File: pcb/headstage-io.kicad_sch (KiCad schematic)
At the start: 2 parts, among them J1 BSE-040-01-X-D-A

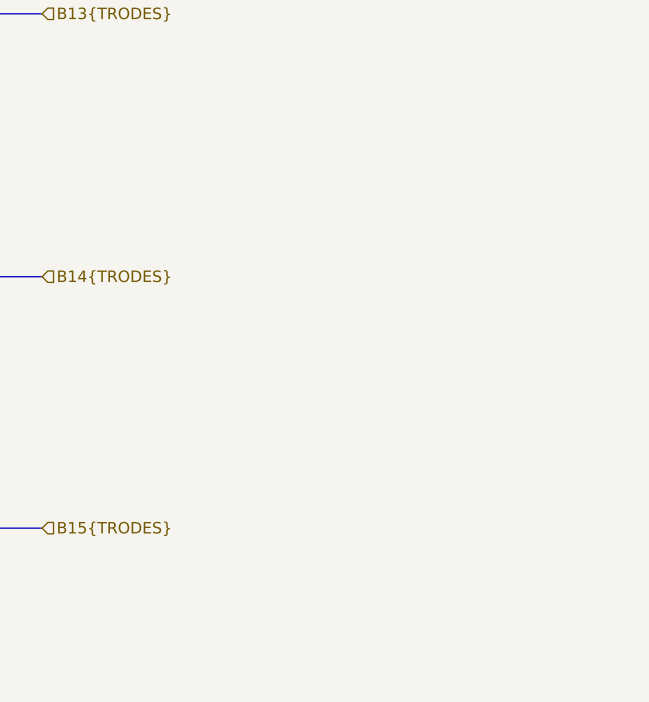
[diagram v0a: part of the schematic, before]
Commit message: Remove battery power option
- This device needs user IO
- Battery power means there would need to be a touch screen or wireless
  connection. Too complex.
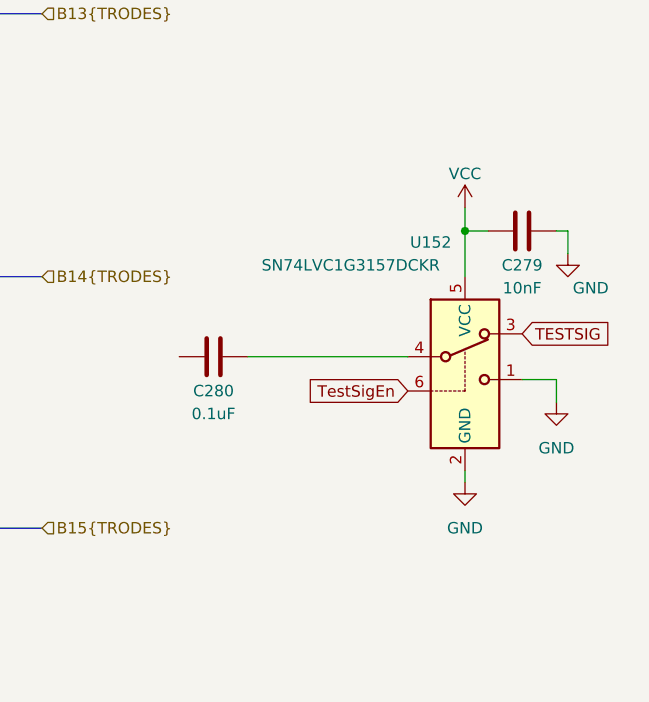
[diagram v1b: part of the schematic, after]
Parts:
- added C279: 10nF, Capacitor_SMD:C_0402_1005Metric, symbol Device:C
- added C280: 0.1uF, Capacitor_SMD:C_0402_1005Metric, symbol Device:C
- added U152: SN74LVC1G3157DCKR, Package_TO_SOT_SMD:SOT-363_SC-70-6, symbol open-ephys:SN74LVC1G3157DCKR
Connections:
- net GND: now also C279.2, U152.1, U152.2 (GND)
- new net: C280.2, U152.4
- new net TESTSIG: U152.3
- new net TestSigEn: U152.6
- new net VCC: C279.1, U152.5 (VCC)

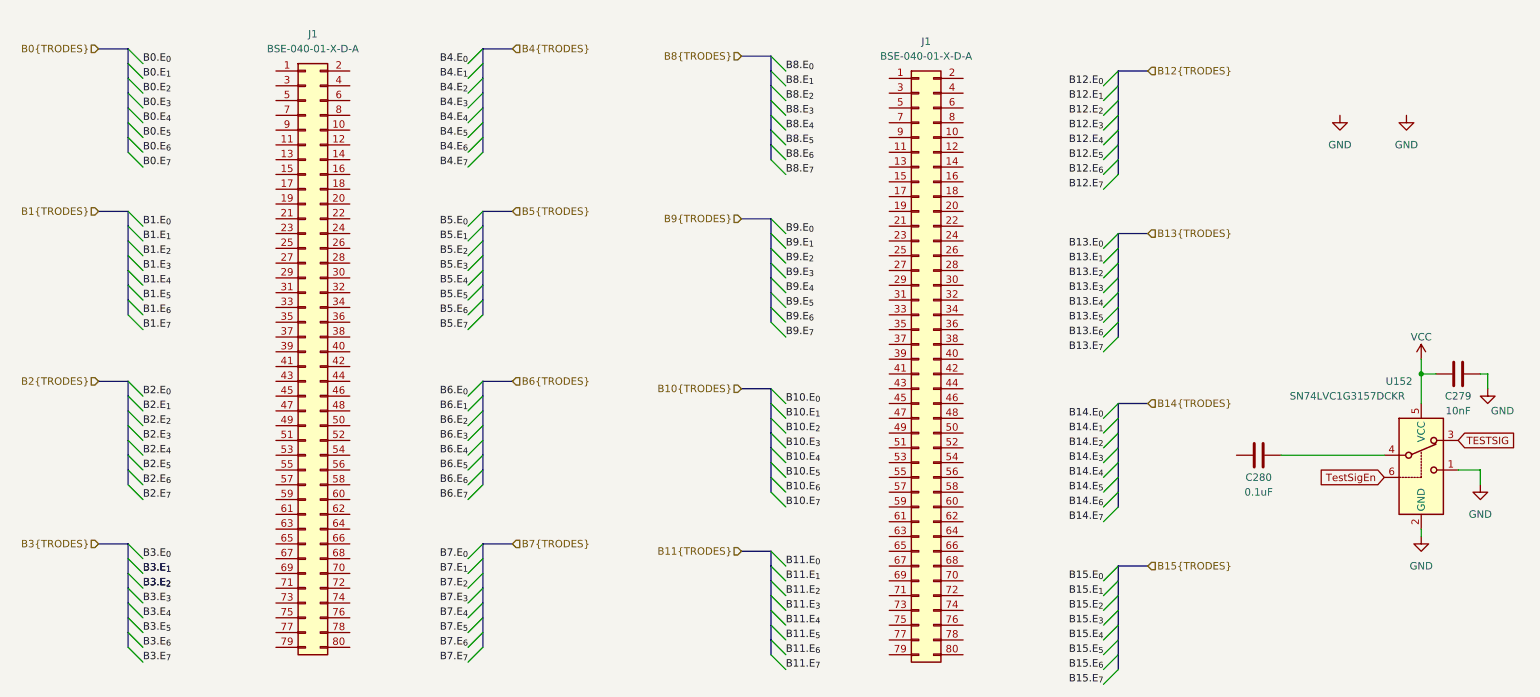
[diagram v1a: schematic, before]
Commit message: Finished schematic, started routing
- There is a 8-channel motif that will need to be copied 16x on the
  board. I'm not sure the most efficient way to do this.
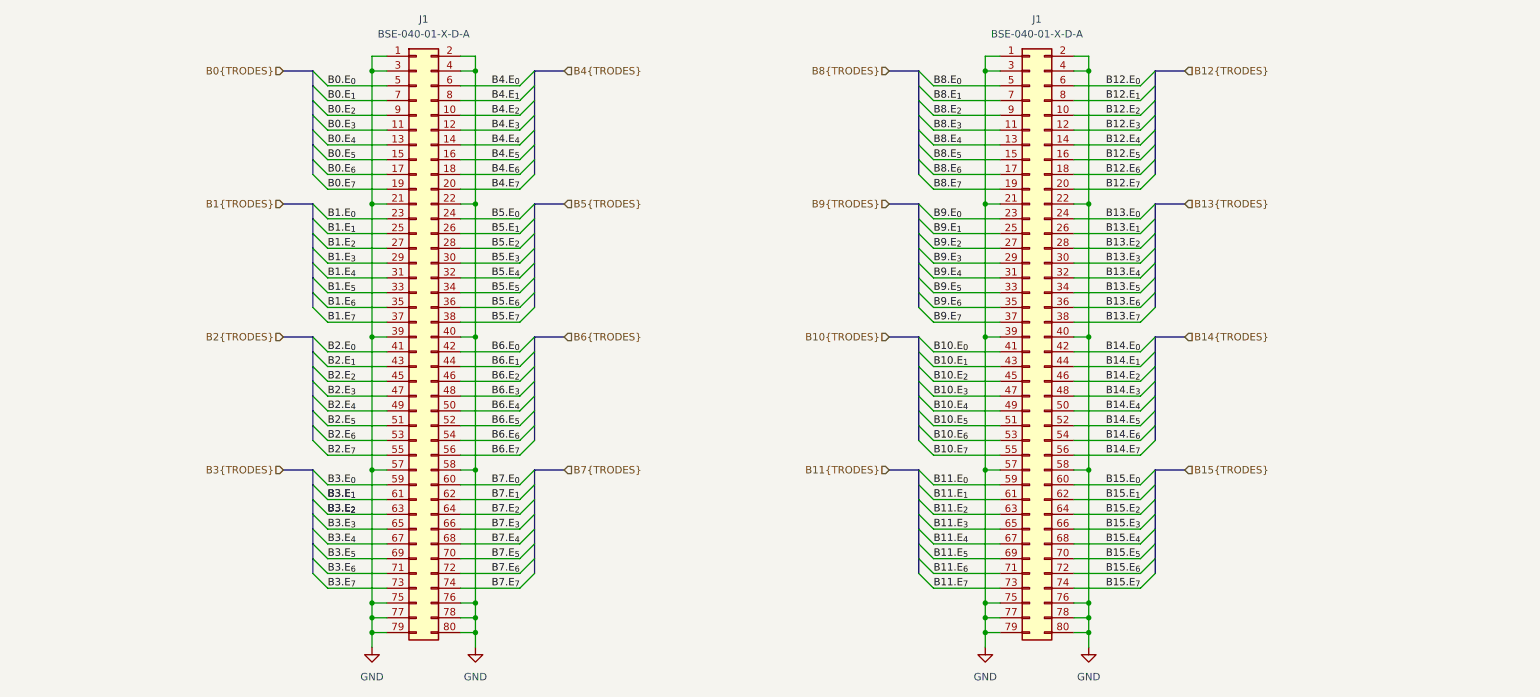
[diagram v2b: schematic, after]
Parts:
- removed C279: 10nF, Capacitor_SMD:C_0402_1005Metric, symbol Device:C
- removed C280: 0.1uF, Capacitor_SMD:C_0402_1005Metric, symbol Device:C
- removed U152: SN74LVC1G3157DCKR, Package_TO_SOT_SMD:SOT-363_SC-70-6, symbol open-ephys:SN74LVC1G3157DCKR
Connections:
- net B0.E_{0}: now also J1.5 (Pin_5)
- net B0.E_{1}: now also J1.7 (Pin_7)
- net B0.E_{2}: now also J1.9 (Pin_9)
- net B0.E_{3}: now also J1.11 (Pin_11)
- net B0.E_{4}: now also J1.13 (Pin_13)
- net B0.E_{5}: now also J1.15 (Pin_15)
- net B0.E_{6}: now also J1.17 (Pin_17)
- net B0.E_{7}: now also J1.19 (Pin_19)
- net B1.E_{0}: now also J1.23 (Pin_23)
- net B1.E_{1}: now also J1.25 (Pin_25)
- net B1.E_{2}: now also J1.27 (Pin_27)
- net B1.E_{3}: now also J1.29 (Pin_29)
- net B1.E_{4}: now also J1.31 (Pin_31)
- net B1.E_{5}: now also J1.33 (Pin_33)
- net B1.E_{6}: now also J1.35 (Pin_35)
- net B1.E_{7}: now also J1.37 (Pin_37)
- net B10.E_{0}: now also J1.41 (Pin_41)
- net B10.E_{1}: now also J1.43 (Pin_43)
- net B10.E_{2}: now also J1.45 (Pin_45)
- net B10.E_{3}: now also J1.47 (Pin_47)
- net B10.E_{4}: now also J1.49 (Pin_49)
- net B10.E_{5}: now also J1.51 (Pin_51)
- net B10.E_{6}: now also J1.53 (Pin_53)
- net B10.E_{7}: now also J1.55 (Pin_55)
- net B11.E_{0}: now also J1.59 (Pin_59)
- net B11.E_{1}: now also J1.61 (Pin_61)
- net B11.E_{2}: now also J1.63 (Pin_63)
- net B11.E_{3}: now also J1.65 (Pin_65)
- net B11.E_{4}: now also J1.67 (Pin_67)
- net B11.E_{5}: now also J1.69 (Pin_69)
- net B11.E_{6}: now also J1.71 (Pin_71)
- net B11.E_{7}: now also J1.73 (Pin_73)
- net B12.E_{0}: now also J1.6 (Pin_6)
- net B12.E_{1}: now also J1.8 (Pin_8)
- net B12.E_{2}: now also J1.10 (Pin_10)
- net B12.E_{3}: now also J1.12 (Pin_12)
- net B12.E_{4}: now also J1.14 (Pin_14)
- net B12.E_{5}: now also J1.16 (Pin_16)
- net B12.E_{6}: now also J1.18 (Pin_18)
- net B12.E_{7}: now also J1.20 (Pin_20)
- net B13.E_{0}: now also J1.24 (Pin_24)
- net B13.E_{1}: now also J1.26 (Pin_26)
- net B13.E_{2}: now also J1.28 (Pin_28)
- net B13.E_{3}: now also J1.30 (Pin_30)
- net B13.E_{4}: now also J1.32 (Pin_32)
- net B13.E_{5}: now also J1.34 (Pin_34)
- net B13.E_{6}: now also J1.36 (Pin_36)
- net B13.E_{7}: now also J1.38 (Pin_38)
- net B14.E_{0}: now also J1.42 (Pin_42)
- net B14.E_{1}: now also J1.44 (Pin_44)
- net B14.E_{2}: now also J1.46 (Pin_46)
- net B14.E_{3}: now also J1.48 (Pin_48)
- net B14.E_{4}: now also J1.50 (Pin_50)
- net B14.E_{5}: now also J1.52 (Pin_52)
- net B14.E_{6}: now also J1.54 (Pin_54)
- net B14.E_{7}: now also J1.56 (Pin_56)
- net B15.E_{0}: now also J1.60 (Pin_60)
- net B15.E_{1}: now also J1.62 (Pin_62)
- net B15.E_{2}: now also J1.64 (Pin_64)
- net B15.E_{3}: now also J1.66 (Pin_66)
- net B15.E_{4}: now also J1.68 (Pin_68)
- net B15.E_{5}: now also J1.70 (Pin_70)
- net B15.E_{6}: now also J1.72 (Pin_72)
- net B15.E_{7}: now also J1.74 (Pin_74)
- net B2.E_{0}: now also J1.41 (Pin_41)
- net B2.E_{1}: now also J1.43 (Pin_43)
- net B2.E_{2}: now also J1.45 (Pin_45)
- net B2.E_{3}: now also J1.47 (Pin_47)
- net B2.E_{4}: now also J1.49 (Pin_49)
- net B2.E_{5}: now also J1.51 (Pin_51)
- net B2.E_{6}: now also J1.53 (Pin_53)
- net B2.E_{7}: now also J1.55 (Pin_55)
- net B3.E_{0}: now also J1.59 (Pin_59)
- net B3.E_{1}: now also J1.61 (Pin_61)
- net B3.E_{2}: now also J1.63 (Pin_63)
- net B3.E_{3}: now also J1.65 (Pin_65)
- net B3.E_{4}: now also J1.67 (Pin_67)
- net B3.E_{5}: now also J1.69 (Pin_69)
- net B3.E_{6}: now also J1.71 (Pin_71)
- net B3.E_{7}: now also J1.73 (Pin_73)
- net B4.E_{0}: now also J1.6 (Pin_6)
- net B4.E_{1}: now also J1.8 (Pin_8)
- net B4.E_{2}: now also J1.10 (Pin_10)
- net B4.E_{3}: now also J1.12 (Pin_12)
- net B4.E_{4}: now also J1.14 (Pin_14)
- net B4.E_{5}: now also J1.16 (Pin_16)
- net B4.E_{6}: now also J1.18 (Pin_18)
- net B4.E_{7}: now also J1.20 (Pin_20)
- net B5.E_{0}: now also J1.24 (Pin_24)
- net B5.E_{1}: now also J1.26 (Pin_26)
- net B5.E_{2}: now also J1.28 (Pin_28)
- net B5.E_{3}: now also J1.30 (Pin_30)
- net B5.E_{4}: now also J1.32 (Pin_32)
- net B5.E_{5}: now also J1.34 (Pin_34)
- net B5.E_{6}: now also J1.36 (Pin_36)
- net B5.E_{7}: now also J1.38 (Pin_38)
- net B6.E_{0}: now also J1.42 (Pin_42)
- net B6.E_{1}: now also J1.44 (Pin_44)
- net B6.E_{2}: now also J1.46 (Pin_46)
- net B6.E_{3}: now also J1.48 (Pin_48)
- net B6.E_{4}: now also J1.50 (Pin_50)
- net B6.E_{5}: now also J1.52 (Pin_52)
- net B6.E_{6}: now also J1.54 (Pin_54)
- net B6.E_{7}: now also J1.56 (Pin_56)
- net B7.E_{0}: now also J1.60 (Pin_60)
- net B7.E_{1}: now also J1.62 (Pin_62)
- net B7.E_{2}: now also J1.64 (Pin_64)
- net B7.E_{3}: now also J1.66 (Pin_66)
- net B7.E_{4}: now also J1.68 (Pin_68)
- net B7.E_{5}: now also J1.70 (Pin_70)
- net B7.E_{6}: now also J1.72 (Pin_72)
- net B7.E_{7}: now also J1.74 (Pin_74)
- net B8.E_{0}: now also J1.5 (Pin_5)
- net B8.E_{1}: now also J1.7 (Pin_7)
- net B8.E_{2}: now also J1.9 (Pin_9)
- net B8.E_{3}: now also J1.11 (Pin_11)
- net B8.E_{4}: now also J1.13 (Pin_13)
- net B8.E_{5}: now also J1.15 (Pin_15)
- net B8.E_{6}: now also J1.17 (Pin_17)
- net B8.E_{7}: now also J1.19 (Pin_19)
- net B9.E_{0}: now also J1.23 (Pin_23)
- net B9.E_{1}: now also J1.25 (Pin_25)
- net B9.E_{2}: now also J1.27 (Pin_27)
- net B9.E_{3}: now also J1.29 (Pin_29)
- net B9.E_{4}: now also J1.31 (Pin_31)
- net B9.E_{5}: now also J1.33 (Pin_33)
- net B9.E_{6}: now also J1.35 (Pin_35)
- net B9.E_{7}: now also J1.37 (Pin_37)
- net GND: now also J1.1 (Pin_1), J1.1 (Pin_1), J1.2 (Pin_2), J1.2 (Pin_2), J1.21 (Pin_21), J1.21 (Pin_21), J1.22 (Pin_22), J1.22 (Pin_22), J1.3 (Pin_3), J1.3 (Pin_3), J1.39 (Pin_39), J1.39 (Pin_39), J1.4 (Pin_4), J1.4 (Pin_4), J1.40 (Pin_40), J1.40 (Pin_40), J1.57 (Pin_57), J1.57 (Pin_57), J1.58 (Pin_58), J1.58 (Pin_58), J1.75 (Pin_75), J1.75 (Pin_75), J1.76 (Pin_76), J1.76 (Pin_76), J1.77 (Pin_77), J1.77 (Pin_77), J1.78 (Pin_78), J1.78 (Pin_78), J1.79 (Pin_79), J1.79 (Pin_79), J1.80 (Pin_80), J1.80 (Pin_80)
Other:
- moved on the sheet: J1

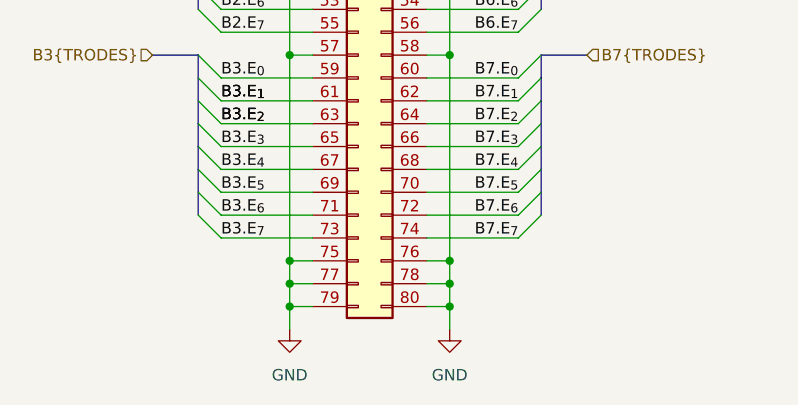
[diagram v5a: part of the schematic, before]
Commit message: Add EEPROM support to headstage interface
- I2C + Power
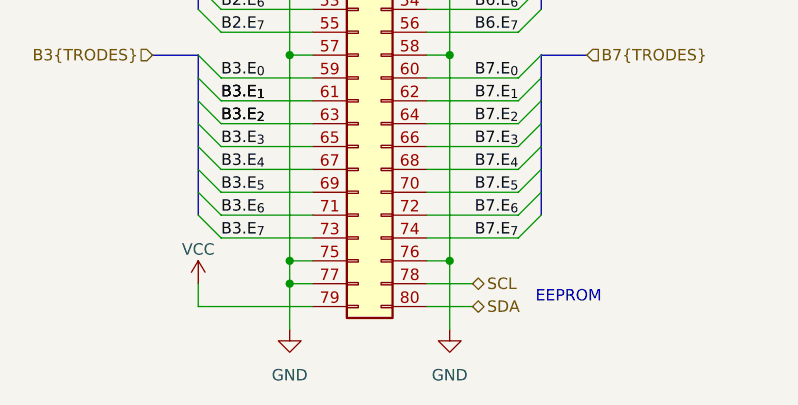
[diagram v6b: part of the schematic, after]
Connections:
- net GND: no longer J1.78 (Pin_78), J1.79 (Pin_79), J1.80 (Pin_80)
- new net SCL: J1.78 (Pin_78)
- new net SDA: J1.80 (Pin_80)
- new net VCC: J1.79 (Pin_79)
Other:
- note added: "EEPROM"
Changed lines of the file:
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@@
 	)
 	(junction
-		(at 96.52 140.97)
-		(diameter 0)
-		(color 0 0 0 0)
-	)
-	(junction
 		(at 201.93 92.71)
 		(diameter 0)
@@
 	)
 	(junction
-		(at 201.93 69.85)
+		(at 78.74 140.97)
 		(diameter 0)
 		(color 0 0 0 0)
 	)
 	(junction
-		(at 78.74 143.51)
+		(at 201.93 69.85)
 		(diameter 0)
 		(color 0 0 0 0)
@@
 		(color 0 0 0 0)
 	)
-	(junction
-		(at 96.52 143.51)
-		(diameter 0)
-		(color 0 0 0 0)
-	)
-	(junction
-		(at 78.74 140.97)
-		(diameter 0)
-		(color 0 0 0 0)
-	)
 	(bus_entry
 		(at 68.58 100.33)
@@
 	(wire
 		(pts
-			(xy 78.74 138.43) (xy 78.74 140.97)
+			(xy 68.58 143.51) (xy 68.58 140.97)
 		)
 		(stroke
@@
 	(wire
 		(pts
+			(xy 93.98 140.97) (xy 99.06 140.97)
+		)
+		(stroke
+			(width 0)
+			(type default)
+		)
+	)
+	(wire
+		(pts
 			(xy 199.39 62.23) (xy 210.82 62.23)
 		)
@@
 	(wire
 		(pts
-			(xy 78.74 143.51) (xy 78.74 146.05)
+			(xy 78.74 138.43) (xy 78.74 140.97)
 		)
 		(stroke
@@
 	(wire
 		(pts
+			(xy 78.74 140.97) (xy 78.74 146.05)
+		)
+		(stroke
+			(width 0)
+			(type default)
+		)
+	)
+	(wire
+		(pts
 			(xy 71.12 130.81) (xy 81.28 130.81)
 		)
@@
 	(wire
 		(pts
+			(xy 93.98 143.51) (xy 99.06 143.51)
+		)
+		(stroke
+			(width 0)
+			(type default)
+		)
+	)
+	(wire
+		(pts
 			(xy 96.52 115.57) (xy 96.52 138.43)
 		)
@@
 	(wire
 		(pts
-			(xy 96.52 140.97) (xy 96.52 143.51)
+			(xy 96.52 138.43) (xy 96.52 146.05)
 		)
 		(stroke
@@
 		)
 	)
-	(wire
-		(pts
-			(xy 78.74 140.97) (xy 78.74 143.51)
-		)
-		(stroke
-			(width 0)
-			(type default)
-		)
-	)
 	(bus
 		(pts
@@
 	(wire
 		(pts
-			(xy 93.98 143.51) (xy 96.52 143.51)
-		)
-		(stroke
-			(width 0)
-			(type default)
-		)
-	)
-	(wire
-		(pts
 			(xy 199.39 120.65) (xy 210.82 120.65)
 		)
@@
 		)
 	)
-	(wire
-		(pts
-			(xy 78.74 143.51) (xy 81.28 143.51)
-		)
-		(stroke
-			(width 0)
-			(type default)
-		)
-	)
 	(bus
 		(pts
@@
 		)
 	)
-	(wire
-		(pts
-			(xy 78.74 140.97) (xy 81.28 140.97)
-		)
-		(stroke
-			(width 0)
-			(type default)
-		)
-	)
 	(bus
 		(pts
@@
 	(wire
 		(pts
-			(xy 93.98 140.97) (xy 96.52 140.97)
-		)
-		(stroke
-			(width 0)
-			(type default)
-		)
-	)
-	(wire
-		(pts
 			(xy 71.12 118.11) (xy 81.28 118.11)
 		)
@@
 	(wire
 		(pts
+			(xy 78.74 140.97) (xy 81.28 140.97)
+		)
+		(stroke
+			(width 0)
+			(type default)
+		)
+	)
+	(wire
+		(pts
 			(xy 199.39 125.73) (xy 210.82 125.73)
 		)
@@
 	(wire
 		(pts
+			(xy 81.28 143.51) (xy 68.58 143.51)
+		)
+		(stroke
+			(width 0)
+			(type default)
+		)
+	)
+	(wire
+		(pts
 			(xy 175.26 57.15) (xy 186.69 57.15)
 		)
@@
 	(wire
 		(pts
-			(xy 96.52 138.43) (xy 96.52 140.97)
-		)
-		(stroke
-			(width 0)
-			(type default)
-		)
-	)
-	(wire
-		(pts
 			(xy 175.26 113.03) (xy 186.69 113.03)
 		)
@@
 	(wire
 		(pts
-			(xy 96.52 143.51) (xy 96.52 146.05)
-		)
-		(stroke
-			(width 0)
-			(type default)
-		)
-	)
-	(wire
-		(pts
 			(xy 199.39 123.19) (xy 210.82 123.19)
 		)
@@
 		)
 	)
+	(text "EEPROM"
+		(exclude_from_sim no)
+		(at 109.728 142.494 0)
+		(effects
+			(font
+				(size 1.27 1.27)
+			)
+		)
+	)
 	(label "B4.E_{3}"
 		(at 104.14 57.15 180)
@@
 		)
 	)
+	(hierarchical_label "SDA"
+		(shape bidirectional)
+		(at 99.06 143.51 0)
+		(fields_autoplaced yes)
+		(effects
+			(font
+				(size 1.27 1.27)
+			)
+			(justify left)
+		)
+	)
 	(hierarchical_label "B6{TRODES}"
 		(shape input)
@@
 		)
 	)
+	(hierarchical_label "SCL"
+		(shape bidirectional)
+		(at 99.06 140.97 0)
+		(fields_autoplaced yes)
+		(effects
+			(font
+				(size 1.27 1.27)
+			)
+			(justify left)
+		)
+	)
 	(hierarchical_label "B1{TRODES}"
 		(shape input)
@@
 					(unit 1)
 				)
+			)
+		)
+	)
+	(symbol
+		(lib_id "power:VCC")
+		(at 68.58 140.97 0)
+		(mirror y)
+		(unit 1)
+		(exclude_from_sim no)
+		(in_bom yes)
+		(on_board yes)
+		(dnp no)
+		(property "Reference" "#PWR0774"
+			(at 68.58 144.78 0)
+			(effects
+				(font
+					(size 1.27 1.27)
+				)
+				(hide yes)
+			)
+		)
+		(property "Value" "VCC"
+			(at 68.58 137.16 0)
+			(effects
+				(font
+					(size 1.27 1.27)
+				)
+			)
+		)
+		(property "Footprint" ""
+			(at 68.58 140.97 0)
+			(effects
+				(font
+					(size 1.27 1.27)
+				)
+				(hide yes)
+			)
+		)
+		(property "Datasheet" ""
+			(at 68.58 140.97 0)
+			(effects
+				(font
+					(size 1.27 1.27)
+				)
+				(hide yes)
+			)
+		)
+		(property "Description" "Power symbol creates a global label with name \"VCC\""
+			(at 68.58 140.97 0)
+			(effects
+				(font
+					(size 1.27 1.27)
+				)
+				(hide yes)
+			)
+		)
+		(pin "1"
+		)
+		(instances
+			(project "ephys-test-board"
+				(path "/ffaa6ffd-73fa-4da3-9ff1-78fa7369281f/f2c6d928-7acb-4b4d-942a-bf07e4ec8d7a"
+					(reference "#PWR0774")
+					(unit 1)
+				)

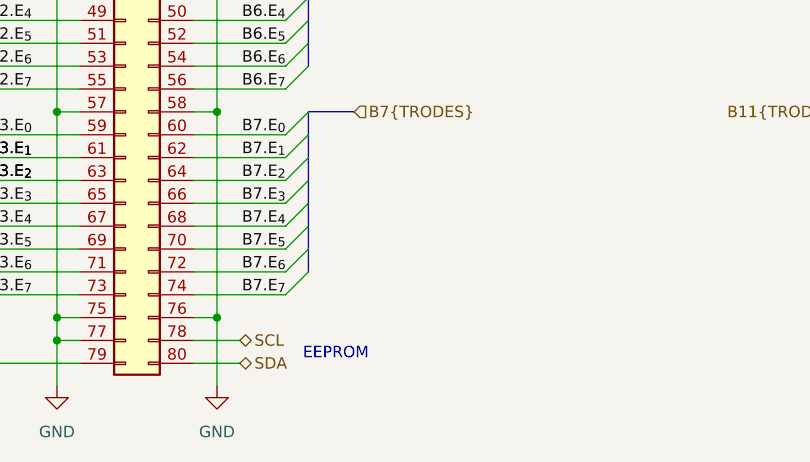
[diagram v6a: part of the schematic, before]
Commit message: More schematic improvements
- Add pullups to i2c bus
- Add test points
- Ready for initial routing
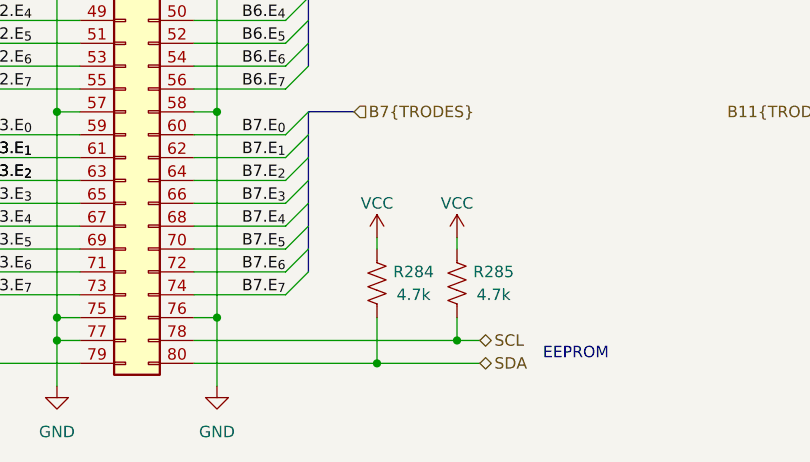
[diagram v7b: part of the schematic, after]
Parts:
- added R284, R285: 4.7k, Resistor_SMD:R_0402_1005Metric, symbol Device:R_US
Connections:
- net SCL: now also R285.2
- net SDA: now also R284.2
- net VCC: now also R284.1, R285.1
